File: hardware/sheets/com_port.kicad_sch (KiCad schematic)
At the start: 16 parts, among them J1 DE9_Pins, J2 Conn_01x03, J3 Conn_01x04, U1 16550, U2 MAX3241, U3 74HCT04, U4 74HCT08, U5 74HCT08, U6 74HCT125

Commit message: Fix all medium design-review findings (M1-M8)
- M1: Supervisor link moved to GPIO4/5 (real UART1 pair); POST -> GPIO6-15
- M2: CNT_RUN = LD0.LD1.LD2 gates every '163 CEP (load-cascade hazard)
- M3: ~WR / IO-M pruned to cpu_core-internal; DRQ2/3 pulled + noted;
  doc S5.2 "as built: 48/48" + S16 updated
- M4: true XT-IDE rev-2 map (A0<->A3 swap): data 0x300, latch 0x301,
  CS1 0x307/0x30F, drive DA0 = bus A3 - matches XTIDE UB "rev 2" type
- M5: COM4 -> bus IRQ2 line (IRQ9 via AT redirect); IRQ10/11/14/15 marked
  off-header; ~REFRESH added to mxbus ISA_CTRL; questions-sidecar superseded
- M6: card_isatest clock tree on unswitched V5RAW (spec S8)
- M7: card_isatest IRQ2-8/DRQ1-3 idle pull-downs (spec S4/S9)
- M8: com_port JP1 selects 16550 RX source (DB9 vs TTL console); 5V note

Rebuilt motherboard + cards; structural ERC = 0; netlist-verified.
Fix log in hardware/notes/design-review-2026-07-03.md (batch 3).

Co-Authored-By: Claude Fable 5 <noreply@anthropic.com>
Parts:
- added JP1: Conn_01x03, symbol Connector_Generic:Conn_01x03
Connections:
- net UART_RXD: now also JP1.2 (Pin_2); no longer J3.3 (Pin_3), U2.9 (R1OUT)
- new net CONSOLE_RXI: J3.3 (Pin_3), JP1.3 (Pin_3)
- new net RXD_RS232: JP1.1 (Pin_1), U2.9 (R1OUT)
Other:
- note added: "JP1 selects UART RX source: 1-2 DB9, 2-3 console"
- note added: "TTL console header J3 (5V levels!): populate on COM1 only;"
- note removed: "TTL console header J3: populate on COM1 only"
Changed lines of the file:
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@@
 		)
 	)
-	(label "UART_RXD"
+	(label "RXD_RS232"
 		(at 209.55 96.52 180)
 		(effects
@@
 		)
 	)
-	(label "UART_RXD"
+	(label "CONSOLE_RXI"
 		(at 162.56 256.54 0)
 		(effects
@@
 	(wire
 		(pts
+			(xy 198.12 251.46)
+			(xy 200.66 251.46)
+		)
+		(stroke
+			(width 0)
+			(type default)
+		)
+	)
+	(label "RXD_RS232"
+		(at 200.66 251.46 0)
+		(effects
+			(font
+				(size 1.27 1.27)
+			)
+		)
+	)
+	(wire
+		(pts
+			(xy 198.12 254)
+			(xy 200.66 254)
+		)
+		(stroke
+			(width 0)
+			(type default)
+		)
+	)
+	(label "UART_RXD"
+		(at 200.66 254 0)
+		(effects
+			(font
+				(size 1.27 1.27)
+			)
+		)
+	)
+	(wire
+		(pts
+			(xy 198.12 256.54)
+			(xy 200.66 256.54)
+		)
+		(stroke
+			(width 0)
+			(type default)
+		)
+	)
+	(label "CONSOLE_RXI"
+		(at 200.66 256.54 0)
+		(effects
+			(font
+				(size 1.27 1.27)
+			)
+		)
+	)
+	(wire
+		(pts
 			(xy 109.22 46.99)
 			(xy 109.22 44.45)
@@
 		)
 	)
-	(text "TTL console header J3: populate on COM1 only"
+	(text "TTL console header J3 (5V levels!): populate on COM1 only;"
 		(at 165.1 248.92 0)
+		(effects
+			(font
+				(size 1.27 1.27)
+			)
+		)
+	)
+	(text "JP1 selects UART RX source: 1-2 DB9, 2-3 console"
+		(at 165.1 246.38 0)
 		(effects
 			(font
@@
 		(instances
 			(project "mini-xt"
-				(path "/ccbe75bb-9744-49b2-888c-84927206f4cb/8e7cca78-92b8-4b9c-92ee-4cac30ac05c6"
+				(path "/9d1a32b9-fdc3-4ebf-878d-e57919a1b88e/d152d23e-9d86-45b7-b645-f2d479dedc69"
 					(reference "U501")
 					(unit 1)
 				)
-				(path "/ccbe75bb-9744-49b2-888c-84927206f4cb/79534d9d-03a1-4a2b-887d-32a67c7415f7"
+				(path "/9d1a32b9-fdc3-4ebf-878d-e57919a1b88e/601a6186-0950-41f8-b453-75d15477f9d0"
 					(reference "U601")
 					(unit 1)
@@
 		(instances
 			(project "mini-xt"
-				(path "/ccbe75bb-9744-49b2-888c-84927206f4cb/8e7cca78-92b8-4b9c-92ee-4cac30ac05c6"
+				(path "/9d1a32b9-fdc3-4ebf-878d-e57919a1b88e/d152d23e-9d86-45b7-b645-f2d479dedc69"
 					(reference "OSC501")
 					(unit 1)
 				)
-				(path "/ccbe75bb-9744-49b2-888c-84927206f4cb/79534d9d-03a1-4a2b-887d-32a67c7415f7"
+				(path "/9d1a32b9-fdc3-4ebf-878d-e57919a1b88e/601a6186-0950-41f8-b453-75d15477f9d0"
 					(reference "OSC601")
 					(unit 1)
@@
 		(instances
 			(project "mini-xt"
-				(path "/ccbe75bb-9744-49b2-888c-84927206f4cb/8e7cca78-92b8-4b9c-92ee-4cac30ac05c6"
+				(path "/9d1a32b9-fdc3-4ebf-878d-e57919a1b88e/d152d23e-9d86-45b7-b645-f2d479dedc69"
 					(reference "U503")
 					(unit 1)
 				)
-				(path "/ccbe75bb-9744-49b2-888c-84927206f4cb/79534d9d-03a1-4a2b-887d-32a67c7415f7"
+				(path "/9d1a32b9-fdc3-4ebf-878d-e57919a1b88e/601a6186-0950-41f8-b453-75d15477f9d0"
 					(reference "U603")
 					(unit 1)
@@
 		(instances
 			(project "mini-xt"
-				(path "/ccbe75bb-9744-49b2-888c-84927206f4cb/8e7cca78-92b8-4b9c-92ee-4cac30ac05c6"
+				(path "/9d1a32b9-fdc3-4ebf-878d-e57919a1b88e/d152d23e-9d86-45b7-b645-f2d479dedc69"
 					(reference "J502")
 					(unit 1)
 				)
-				(path "/ccbe75bb-9744-49b2-888c-84927206f4cb/79534d9d-03a1-4a2b-887d-32a67c7415f7"
+				(path "/9d1a32b9-fdc3-4ebf-878d-e57919a1b88e/601a6186-0950-41f8-b453-75d15477f9d0"
 					(reference "J602")
 					(unit 1)
@@
 		(instances
 			(project "mini-xt"
-				(path "/ccbe75bb-9744-49b2-888c-84927206f4cb/8e7cca78-92b8-4b9c-92ee-4cac30ac05c6"
+				(path "/9d1a32b9-fdc3-4ebf-878d-e57919a1b88e/d152d23e-9d86-45b7-b645-f2d479dedc69"
 					(reference "U504")
 					(unit 1)
 				)
-				(path "/ccbe75bb-9744-49b2-888c-84927206f4cb/79534d9d-03a1-4a2b-887d-32a67c7415f7"
+				(path "/9d1a32b9-fdc3-4ebf-878d-e57919a1b88e/601a6186-0950-41f8-b453-75d15477f9d0"
 					(reference "U604")
 					(unit 1)
@@
 		(instances
 			(project "mini-xt"
-				(path "/ccbe75bb-9744-49b2-888c-84927206f4cb/8e7cca78-92b8-4b9c-92ee-4cac30ac05c6"
+				(path "/9d1a32b9-fdc3-4ebf-878d-e57919a1b88e/d152d23e-9d86-45b7-b645-f2d479dedc69"
 					(reference "U505")
 					(unit 1)
 				)
-				(path "/ccbe75bb-9744-49b2-888c-84927206f4cb/79534d9d-03a1-4a2b-887d-32a67c7415f7"
+				(path "/9d1a32b9-fdc3-4ebf-878d-e57919a1b88e/601a6186-0950-41f8-b453-75d15477f9d0"
 					(reference "U605")
 					(unit 1)
@@
 		(instances
 			(project "mini-xt"
-				(path "/ccbe75bb-9744-49b2-888c-84927206f4cb/8e7cca78-92b8-4b9c-92ee-4cac30ac05c6"
+				(path "/9d1a32b9-fdc3-4ebf-878d-e57919a1b88e/d152d23e-9d86-45b7-b645-f2d479dedc69"
 					(reference "U506")
 					(unit 1)
 				)
-				(path "/ccbe75bb-9744-49b2-888c-84927206f4cb/79534d9d-03a1-4a2b-887d-32a67c7415f7"
+				(path "/9d1a32b9-fdc3-4ebf-878d-e57919a1b88e/601a6186-0950-41f8-b453-75d15477f9d0"
 					(reference "U606")
 					(unit 1)
@@
 		(instances
 			(project "mini-xt"
-				(path "/ccbe75bb-9744-49b2-888c-84927206f4cb/8e7cca78-92b8-4b9c-92ee-4cac30ac05c6"
+				(path "/9d1a32b9-fdc3-4ebf-878d-e57919a1b88e/d152d23e-9d86-45b7-b645-f2d479dedc69"
 					(reference "U502")
 					(unit 1)
 				)
-				(path "/ccbe75bb-9744-49b2-888c-84927206f4cb/79534d9d-03a1-4a2b-887d-32a67c7415f7"
+				(path "/9d1a32b9-fdc3-4ebf-878d-e57919a1b88e/601a6186-0950-41f8-b453-75d15477f9d0"
 					(reference "U602")
 					(unit 1)
@@
 		(instances
 			(project "mini-xt"
-				(path "/ccbe75bb-9744-49b2-888c-84927206f4cb/8e7cca78-92b8-4b9c-92ee-4cac30ac05c6"
+				(path "/9d1a32b9-fdc3-4ebf-878d-e57919a1b88e/d152d23e-9d86-45b7-b645-f2d479dedc69"
 					(reference "C503")
 					(unit 1)
 				)
-				(path "/ccbe75bb-9744-49b2-888c-84927206f4cb/79534d9d-03a1-4a2b-887d-32a67c7415f7"
+				(path "/9d1a32b9-fdc3-4ebf-878d-e57919a1b88e/601a6186-0950-41f8-b453-75d15477f9d0"
 					(reference "C603")
 					(unit 1)
@@
 		(instances
 			(project "mini-xt"
-				(path "/ccbe75bb-9744-49b2-888c-84927206f4cb/8e7cca78-92b8-4b9c-92ee-4cac30ac05c6"
+				(path "/9d1a32b9-fdc3-4ebf-878d-e57919a1b88e/d152d23e-9d86-45b7-b645-f2d479dedc69"
 					(reference "C504")
 					(unit 1)
 				)
-				(path "/ccbe75bb-9744-49b2-888c-84927206f4cb/79534d9d-03a1-4a2b-887d-32a67c7415f7"
+				(path "/9d1a32b9-fdc3-4ebf-878d-e57919a1b88e/601a6186-0950-41f8-b453-75d15477f9d0"
 					(reference "C604")
 					(unit 1)
@@
 		(instances
 			(project "mini-xt"
-				(path "/ccbe75bb-9744-49b2-888c-84927206f4cb/8e7cca78-92b8-4b9c-92ee-4cac30ac05c6"
+				(path "/9d1a32b9-fdc3-4ebf-878d-e57919a1b88e/d152d23e-9d86-45b7-b645-f2d479dedc69"
 					(reference "C505")
 					(unit 1)
 				)
-				(path "/ccbe75bb-9744-49b2-888c-84927206f4cb/79534d9d-03a1-4a2b-887d-32a67c7415f7"
+				(path "/9d1a32b9-fdc3-4ebf-878d-e57919a1b88e/601a6186-0950-41f8-b453-75d15477f9d0"
 					(reference "C605")
 					(unit 1)
@@
 		(instances
 			(project "mini-xt"
-				(path "/ccbe75bb-9744-49b2-888c-84927206f4cb/8e7cca78-92b8-4b9c-92ee-4cac30ac05c6"
+				(path "/9d1a32b9-fdc3-4ebf-878d-e57919a1b88e/d152d23e-9d86-45b7-b645-f2d479dedc69"
 					(reference "C506")
 					(unit 1)
 				)
-				(path "/ccbe75bb-9744-49b2-888c-84927206f4cb/79534d9d-03a1-4a2b-887d-32a67c7415f7"
+				(path "/9d1a32b9-fdc3-4ebf-878d-e57919a1b88e/601a6186-0950-41f8-b453-75d15477f9d0"
 					(reference "C606")
 					(unit 1)
@@
 		(instances
 			(project "mini-xt"
-				(path "/ccbe75bb-9744-49b2-888c-84927206f4cb/8e7cca78-92b8-4b9c-92ee-4cac30ac05c6"
+				(path "/9d1a32b9-fdc3-4ebf-878d-e57919a1b88e/d152d23e-9d86-45b7-b645-f2d479dedc69"
 					(reference "J501")
 					(unit 1)
 				)
-				(path "/ccbe75bb-9744-49b2-888c-84927206f4cb/79534d9d-03a1-4a2b-887d-32a67c7415f7"
+				(path "/9d1a32b9-fdc3-4ebf-878d-e57919a1b88e/601a6186-0950-41f8-b453-75d15477f9d0"
 					(reference "J601")
 					(unit 1)
@@
 		(instances
 			(project "mini-xt"
-				(path "/ccbe75bb-9744-49b2-888c-84927206f4cb/8e7cca78-92b8-4b9c-92ee-4cac30ac05c6"
+				(path "/9d1a32b9-fdc3-4ebf-878d-e57919a1b88e/d152d23e-9d86-45b7-b645-f2d479dedc69"
 					(reference "J503")
 					(unit 1)
 				)
-				(path "/ccbe75bb-9744-49b2-888c-84927206f4cb/79534d9d-03a1-4a2b-887d-32a67c7415f7"
+				(path "/9d1a32b9-fdc3-4ebf-878d-e57919a1b88e/601a6186-0950-41f8-b453-75d15477f9d0"
 					(reference "J603")
+					(unit 1)
+				)
+			)
+		)
+	)
+	(symbol
+		(lib_id "Connector_Generic:Conn_01x03")
+		(at 203.2 254 0)
+		(unit 1)
+		(exclude_from_sim no)
+		(in_bom yes)
+		(on_board yes)
+		(dnp no)
+		(fields_autoplaced yes)
+		(property "Reference" "JP1"
+			(at 203.2 248.92 0)
+			(effects
+				(font
+					(size 1.27 1.27)
+				)
+			)
+		)
+		(property "Value" "Conn_01x03"
+			(at 203.2 259.08 0)
+			(effects
+				(font
+					(size 1.27 1.27)
+				)
+			)
+		)
+		(property "Footprint" ""
+			(at 203.2 254 0)
+			(effects
+				(font
+					(size 1.27 1.27)
+				)
+				(hide yes)
+			)
+		)
+		(pin "1"
+		)
+		(pin "2"
+		)
+		(pin "3"
+		)
+		(instances
+			(project "mini-xt"
+				(path "/9d1a32b9-fdc3-4ebf-878d-e57919a1b88e/d152d23e-9d86-45b7-b645-f2d479dedc69"
+					(reference "JP501")
+					(unit 1)
+				)
+				(path "/9d1a32b9-fdc3-4ebf-878d-e57919a1b88e/601a6186-0950-41f8-b453-75d15477f9d0"
+					(reference "JP601")
 					(unit 1)
 				)
@@
 		(instances
 			(project "mini-xt"
-				(path "/ccbe75bb-9744-49b2-888c-84927206f4cb/8e7cca78-92b8-4b9c-92ee-4cac30ac05c6"
+				(path "/9d1a32b9-fdc3-4ebf-878d-e57919a1b88e/d152d23e-9d86-45b7-b645-f2d479dedc69"
 					(reference "C501")
 					(unit 1)
 				)
-				(path "/ccbe75bb-9744-49b2-888c-84927206f4cb/79534d9d-03a1-4a2b-887d-32a67c7415f7"
+				(path "/9d1a32b9-fdc3-4ebf-878d-e57919a1b88e/601a6186-0950-41f8-b453-75d15477f9d0"
 					(reference "C601")
 					(unit 1)
@@
 		(instances
 			(project "mini-xt"
-				(path "/ccbe75bb-9744-49b2-888c-84927206f4cb/8e7cca78-92b8-4b9c-92ee-4cac30ac05c6"
+				(path "/9d1a32b9-fdc3-4ebf-878d-e57919a1b88e/d152d23e-9d86-45b7-b645-f2d479dedc69"
 					(reference "C502")
 					(unit 1)
 				)
-				(path "/ccbe75bb-9744-49b2-888c-84927206f4cb/79534d9d-03a1-4a2b-887d-32a67c7415f7"
+				(path "/9d1a32b9-fdc3-4ebf-878d-e57919a1b88e/601a6186-0950-41f8-b453-75d15477f9d0"
 					(reference "C602")
 					(unit 1)

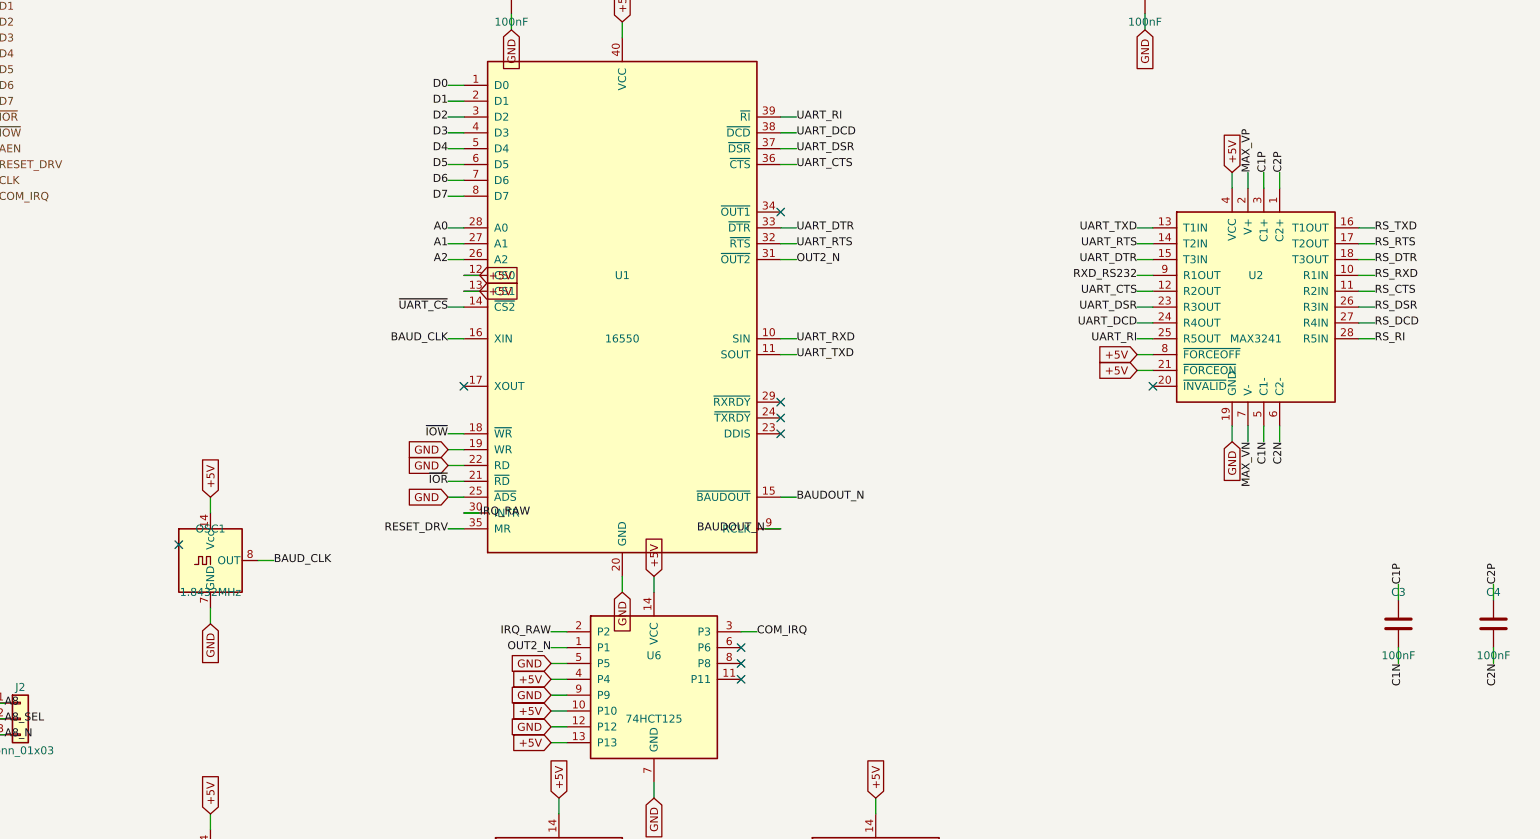
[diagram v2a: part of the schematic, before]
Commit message: JLCPCB sourcing pass: verify pinouts, LCSC part numbers, SMD build
Custom-symbol verification (open-questions Q5 resolved):
- MAX3241 symbol was wrong on nearly every pin and used MAX3243-style
  control names; regenerated to the real SSOP-28 pinout (SHDN#/EN#/
  R1OUTB/R2OUTB) and com_port rewired -- EN# must be GROUNDED (the old
  ~FORCEON-high would have disabled the receivers on real silicon)
- DS12C887 symbol wrong on 4 pins (DS=17, RESET#=18, IRQ#=19, SQW=23)

Sourcing (every part checked against the JLC DB; ~45 line items):
- New tools/parts.py maps (lib_id, value) -> LCSC; build.py applies it as
  an 'LCSC Part Num' property on every component (384 across the project)
- Sheets stay generic; stock-forced substitutions bound in the map:
  '374->'574 (parallel rewired), '163->'161, '157->HC157 (+HCT-buffered
  3.3V selects, I0/I1 swapped), '02->HC02, TCM809->MCP809, 2N3904->MMBT3904
- bus_mcu address counters moved to the 3.3V domain (HC161 on 3V3_BUS,
  loaded from MCU-side MD0-7; HCT244s read the 3.3V outputs at TTL Vih)
- 14.318 XOs are 3.3V-only parts: powered from 3V3, squared up via spare
  HCT gates (cpu_core U13, card_isatest U19)
- COM baud reference is now a 1.8432MHz crystal on the 16C550's XIN/XOUT
  (3.3V-only oscillators vs a 5V-only soft card)
- Supervisor QSPI header replaced with a real W25Q128JVSIQ
- Socket policy (fab installs sockets): V20 DIP-40, SRAM DIP-32 (no 5V
  512Kx8 SRAM at JLC at all), DS12C887 DIP-24, female headers for modules

Docs: CLAUDE.md fabrication-constraints section (SMD, 100x100mm, generic-
symbols rule, voltage-domain rule); README + hardware/README fab notes;
notes/jlcpcb-sourcing.md (decisions, thin-stock flags, not-at-JLC list);
stale questions-sidecar.md collapsed to its supersession record.

Rebuilt motherboard + cards: structural ERC 0, byte-identical rebuilds.

Co-Authored-By: Claude Fable 5 <noreply@anthropic.com>
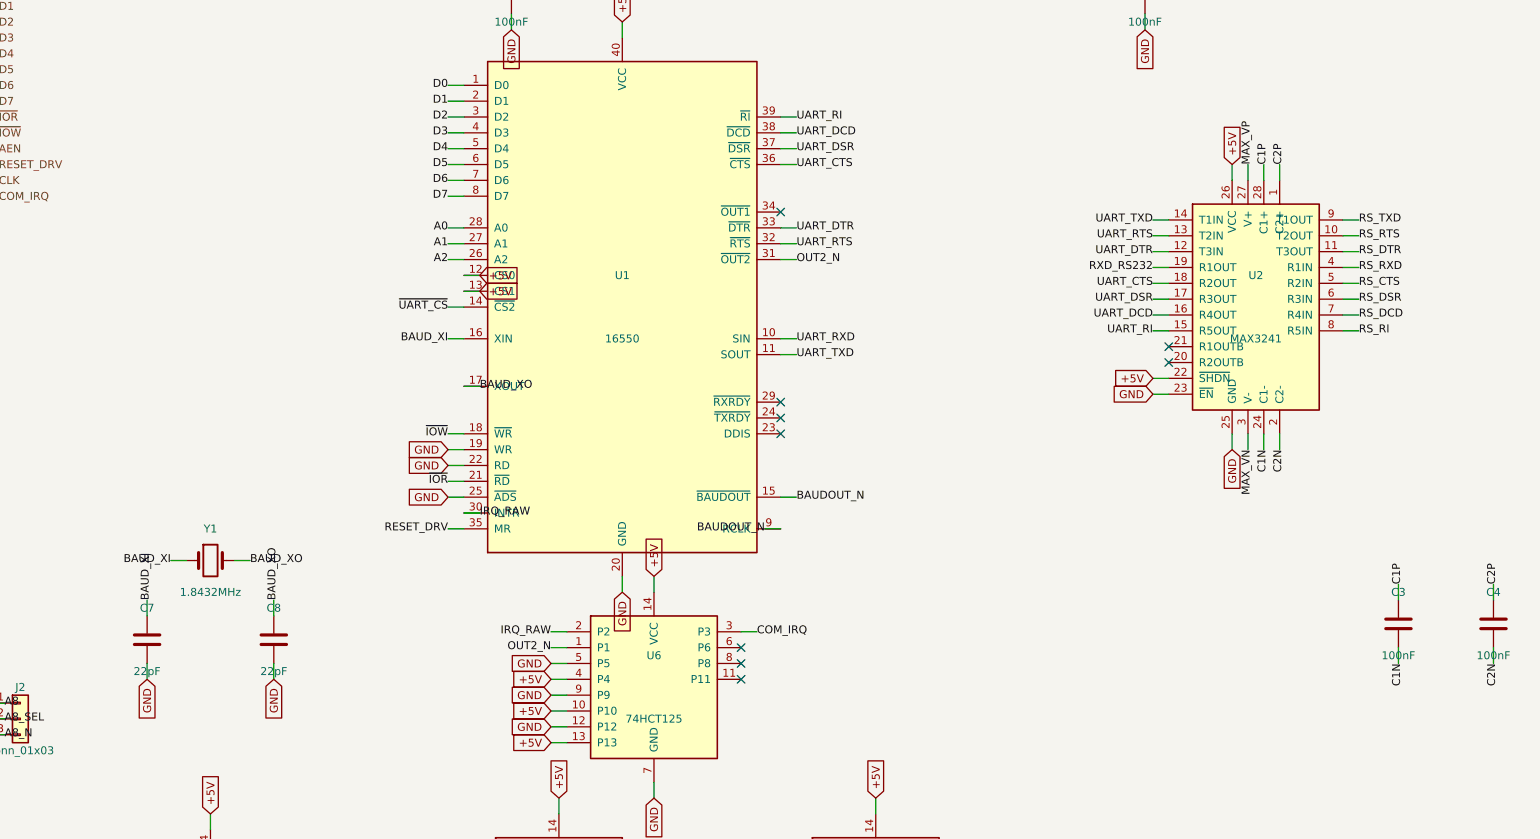
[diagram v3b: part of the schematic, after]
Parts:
- removed J3: Conn_01x04, symbol Connector_Generic:Conn_01x04
- removed OSC1: 1.8432MHz, symbol Oscillator:ACO-xxxMHz
- added C7, C8: 22pF, symbol Device:C
- added JP1: Conn_01x03, symbol Connector_Generic:Conn_01x03
- added Y1: 1.8432MHz, symbol Device:Crystal
- C1, C2, C3, C4, C5, C6: LCSC Part Num (none) -> C14663
- J1: LCSC Part Num (none) -> C141880
- J2: LCSC Part Num (none) -> C2337
- J3: renamed from JP1; value Conn_01x03 -> Conn_01x04; symbol Connector_Generic:Conn_01x03 -> Connector_Generic:Conn_01x04; LCSC Part Num (none) -> C2337
- U1: LCSC Part Num (none) -> C544406
- U2: LCSC Part Num (none) -> C406859
- U3: LCSC Part Num (none) -> C672096
- U4, U5: LCSC Part Num (none) -> C5959
- U6: LCSC Part Num (none) -> C5962
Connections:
- net +5V: now also J3.4 (Pin_4), U2.22 (~{SHDN}), U2.26 (VCC); no longer U2.21 (~{FORCEON}), U2.4 (VCC), U2.8 (~{FORCEOFF})
- net C1N: now also U2.24 (C1-); no longer U2.5 (C1-)
- net C1P: now also U2.28 (C1+); no longer U2.3 (C1+)
- net C2N: now also U2.2 (C2-); no longer U2.6 (C2-)
- net CONSOLE_RXI: now also JP1.3 (Pin_3)
- net GND: now also J3.1 (Pin_1), U2.23 (~{EN}), U2.25 (GND), C7.2, C8.2; no longer U2.19 (GND)
- net MAX_VN: now also U2.3 (V-); no longer U2.7 (V-)
- net MAX_VP: now also U2.27 (V+); no longer U2.2 (V+)
- net RS_CTS: now also U2.5 (R2IN); no longer U2.11 (R2IN)
- net RS_DCD: now also U2.7 (R4IN); no longer U2.27 (R4IN)
- net RS_DSR: now also U2.6 (R3IN); no longer U2.26 (R3IN)
- net RS_DTR: now also U2.11 (T3OUT); no longer U2.18 (T3OUT)
- net RS_RI: now also U2.8 (R5IN); no longer U2.28 (R5IN)
- net RS_RTS: now also U2.10 (T2OUT); no longer U2.17 (T2OUT)
- net RS_RXD: now also U2.4 (R1IN); no longer U2.10 (R1IN)
- net RS_TXD: now also U2.9 (T1OUT); no longer U2.16 (T1OUT)
- net RXD_RS232: now also U2.19 (R1OUT), JP1.1 (Pin_1); no longer J3.1 (Pin_1), U2.9 (R1OUT)
- net UART_CTS: now also U2.18 (R2OUT); no longer U2.12 (R2OUT)
- net UART_DCD: now also U2.16 (R4OUT); no longer U2.24 (R4OUT)
- net UART_DSR: now also U2.17 (R3OUT); no longer U2.23 (R3OUT)
- net UART_DTR: now also U2.12 (T3IN); no longer U2.15 (T3IN)
- net UART_RI: now also U2.15 (R5OUT); no longer U2.25 (R5OUT)
- net UART_RTS: now also U2.13 (T2IN); no longer U2.14 (T2IN)
- net UART_RXD: now also JP1.2 (Pin_2); no longer J3.2 (Pin_2)
- net UART_TXD: now also J3.2 (Pin_2), U2.14 (T1IN); no longer U2.13 (T1IN)
- net BAUD_XO: now reaches U1.17 (XOUT)
- net BAUD_XO: now also C8.1, Y1.2
- net BAUD_CLK renamed BAUD_XI
- net BAUD_XI: now also C7.1, Y1.1
- no-connect marks 14 -> 13

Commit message: COM cards: socket the 16550s (SMD PLCC-44)
The fab reflows a Nextron SMD PLCC-44 socket (LCSC C2828044, ~$0.39) in
the normal SMD pass; the UART installs by hand. One footprint accepts the
active-production TL16C550CFNR (Mouser ~320 pcs), NOS tubes, and period
NS16550AFN pulls (same industry PLCC pinout), and a suspect UART is
diagnosed by swap. MaxLinear's PLCC ST16C550CJ44-F is EOL; TI's reel CFNR
is the active leg. Schematic unchanged (parts.py retarget + comments);
DB9s stay THT (C141880) -- SMD D-subs cost 5-9x and shear pads under
cable torque. Sourcing notes + CLAUDE.md socket policy updated.

Co-Authored-By: Claude Fable 5 <noreply@anthropic.com>
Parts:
- U1: LCSC Part Num C544406 -> C2828044
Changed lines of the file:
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@@
 			)
 		)
-		(property "LCSC Part Num" "C544406"
+		(property "LCSC Part Num" "C2828044"
 			(at 127 101.6 0)
 			(effects
